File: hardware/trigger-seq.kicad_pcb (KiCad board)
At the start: 2 copper layers, 74.5 x 104.6 mm, 64 parts, among them P1 MOTM Power, P2 Euro Power, P4 JACKS_MAIN, P6 pickit header, P7 SWITCH_MAIN, Q1 2N3904, Q2 2N3904, Q3 2N3904, Q4 2N3904, Q5 2N3904, U1 LM78L05, U3 PIC16F15345, U4 LM393, U5 4051, U6 4051, U8 TL072

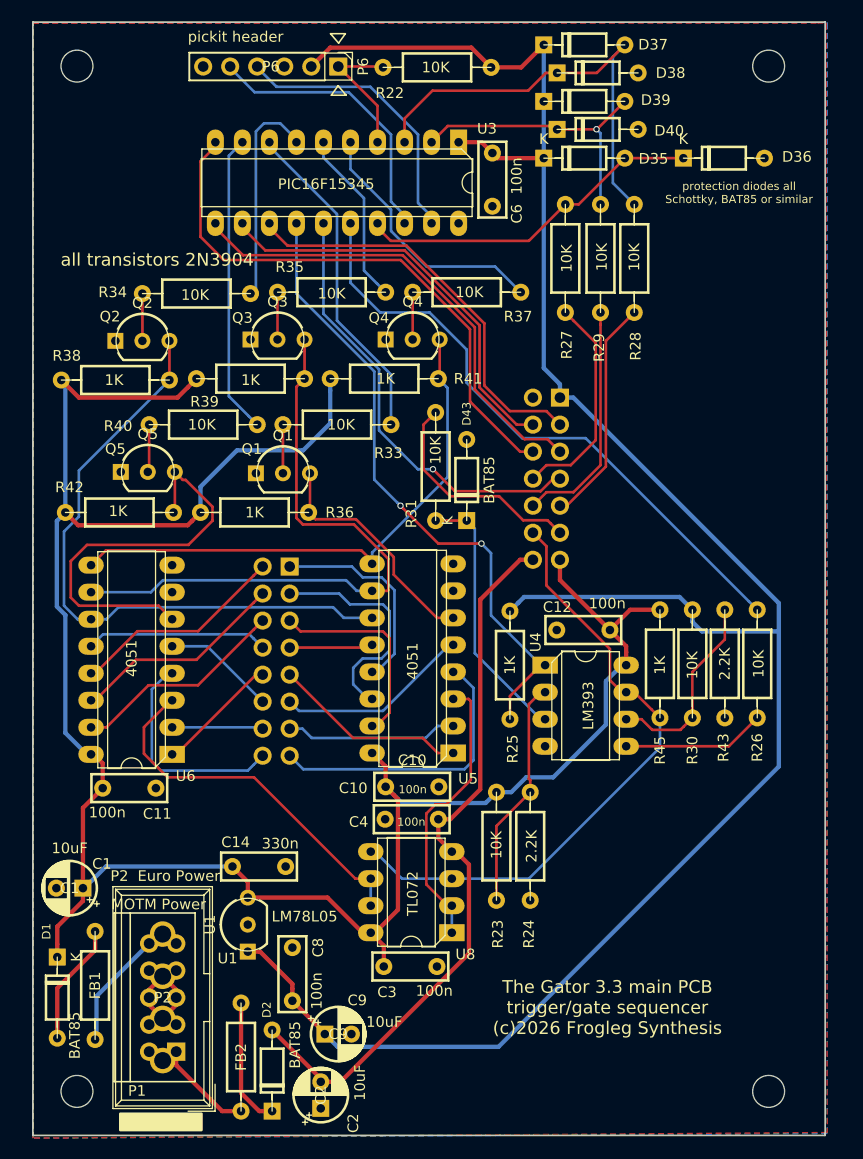
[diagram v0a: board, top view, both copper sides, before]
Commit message: updates to correct firmware to use clock in detection; MCLRE=OFF, corrected bit locations for IOC interrupts.  updates to schematics/layout
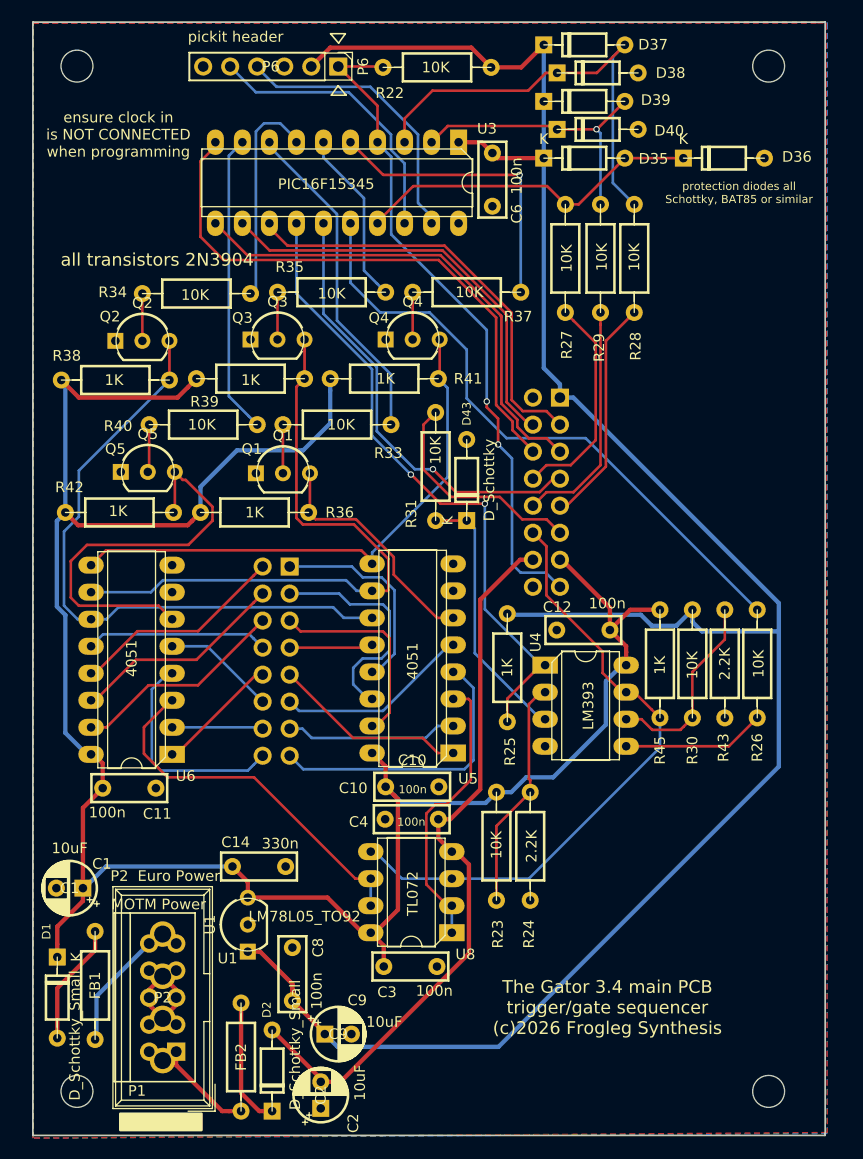
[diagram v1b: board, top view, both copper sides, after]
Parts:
- D1, D2: value BAT85 -> D_Schottky_Small
- D43: value BAT85 -> D_Schottky
- P4: footprint Connector_PinHeader_2.54mm:PinHeader_2x07_P2.54mm_Vertical -> Connector_PinHeader_2.54mm:PinHeader_2x08_P2.54mm_Vertical
- U1: value LM78L05 -> LM78L05_TO92
- moved R25 0.35 mm to (126.2, 106.9)
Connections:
- net 2x8/1x16 renamed 2x8/1x16
- net R/S renamed R/S
- net U/D renamed U/D
- P6 pad 6: (no net) -> unconnected-(P6-Pad6)
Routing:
- net pg: track 12.9 -> 63.1 mm, vias 0 -> 2
- net /main/clock/adr3: track 24.5 -> 28.2 mm, vias 0 -> 1
- net steps: track 44.9 -> 46.5 mm
- net swing: track 53.0 -> 54.4 mm
- net width: track 38.8 -> 40.2 mm
- net rate: track 38.8 -> 40.0 mm
- net Net-(R26-Pad2): track 58.4 -> 59.2 mm
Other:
- board text added: "The Gator 3.4 main PCB trigger/gate sequencer (c)2026 Frogleg Synthesis"
- board text added: "ensure clock in is NOT CONNECTED when programming"
- board text removed: "The Gator 3.3 main PCB trigger/gate sequencer (c)2026 Frogleg Synthesis"

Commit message: updates to schematic properties, nips and tucks
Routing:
- net pg: track 63.1 -> 61.7 mm
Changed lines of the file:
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@@
   (segment (start 124.313 86.976) (end 124.313 87.527) (width 0.25) (layer "F.Cu") (net 26))
   (segment (start 114.481 55.499) (end 110.359 55.499) (width 0.25) (layer "F.Cu") (net 26))
-  (segment (start 110.359 55.499) (end 114.046 59.186) (width 0.25) (layer "F.Cu") (net 26))
+  (segment (start 114.046 56.092) (end 114.046 62.611) (width 0.25) (layer "F.Cu") (net 26))
   (segment (start 124.313 87.527) (end 125.379 88.593) (width 0.25) (layer "F.Cu") (net 26))
+  (segment (start 114.56 55.578) (end 114.046 56.092) (width 0.25) (layer "F.Cu") (net 26))
   (segment (start 125.379 88.593) (end 125.379 91.021) (width 0.25) (layer "F.Cu") (net 26))
-  (segment (start 114.046 59.186) (end 114.046 62.611) (width 0.25) (layer "F.Cu") (net 26))
   (segment (start 114.56 55.578) (end 114.481 55.499) (width 0.25) (layer "F.Cu") (net 26))
   (via (at 125.379 91.021) (size 0.6) (drill 0.4) (layers "F.Cu" "B.Cu") (net 26))
